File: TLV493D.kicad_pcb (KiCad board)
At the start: 2 copper layers, 6 parts, among them U1 TLV493D

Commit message: Add connector
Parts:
- added J1: Conn_01x04_Female, Connector_PinHeader_2.54mm:PinHeader_1x04_P2.54mm_Vertical, F.Cu at (162.0, 113.0)
- R1: value R_Small -> 330
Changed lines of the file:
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@@
-(kicad_pcb (version 20171130) (host pcbnew "(5.1.2-1)-1")
+(kicad_pcb (version 20171130) (host pcbnew "(5.1.4-0-10_14)")
   (general
     (thickness 1.6)
@@
     (tracks 0)
     (zones 0)
-    (modules 6)
+    (modules 7)
     (nets 6)
   )
   (page A4)
+  (title_block
+    (title TLV493D)
+    (date 2019-09-04)
+    (rev 0.1)
+    (company "Electronic Cats")
+    (comment 4 "Andres Sabas")
+  )
   (layers
     (0 F.Cu signal)
@@
       (effects (font (size 1 1) (thickness 0.15)))
     )
-    (fp_text value R_Small (at 0 1.75) (layer F.Fab)
+    (fp_text value 330 (at 0 1.75) (layer F.Fab)
       (effects (font (size 1 1) (thickness 0.15)))
     )
@@
       (at (xyz 0 0 0))
       (scale (xyz 1 1 1))
+      (rotate (xyz 0 0 0))
+    )
+  )
+  (module Connector_PinHeader_2.54mm:PinHeader_1x04_P2.54mm_Vertical (layer F.Cu)
+    (at 162 113.02 270)
+    (descr "Through hole straight pin header, 1x04, 2.54mm pitch, single row")
+    (tags "Through hole pin header THT 1x04 2.54mm single row")
+    (fp_text reference J1 (at 0 -2.33 90) (layer F.SilkS)
+      (effects (font (size 1 1) (thickness 0.15)))
+    )
+    (fp_text value Conn_01x04_Female (at 0 9.95 90) (layer F.Fab)
+      (effects (font (size 1 1) (thickness 0.15)))
+    )
+    (fp_line (start -0.635 -1.27) (end 1.27 -1.27) (layer F.Fab) (width 0.1))
+    (fp_line (start 1.27 -1.27) (end 1.27 8.89) (layer F.Fab) (width 0.1))
+    (fp_line (start 1.27 8.89) (end -1.27 8.89) (layer F.Fab) (width 0.1))
+    (fp_line (start -1.27 8.89) (end -1.27 -0.635) (layer F.Fab) (width 0.1))
+    (fp_line (start -1.27 -0.635) (end -0.635 -1.27) (layer F.Fab) (width 0.1))
+    (fp_line (start -1.33 8.95) (end 1.33 8.95) (layer F.SilkS) (width 0.12))
+    (fp_line (start -1.33 1.27) (end -1.33 8.95) (layer F.SilkS) (width 0.12))
+    (fp_line (start 1.33 1.27) (end 1.33 8.95) (layer F.SilkS) (width 0.12))
+    (fp_line (start -1.33 1.27) (end 1.33 1.27) (layer F.SilkS) (width 0.12))
+    (fp_line (start -1.33 0) (end -1.33 -1.33) (layer F.SilkS) (width 0.12))
+    (fp_line (start -1.33 -1.33) (end 0 -1.33) (layer F.SilkS) (width 0.12))
+    (fp_line (start -1.8 -1.8) (end -1.8 9.4) (layer F.CrtYd) (width 0.05))
+    (fp_line (start -1.8 9.4) (end 1.8 9.4) (layer F.CrtYd) (width 0.05))
+    (fp_line (start 1.8 9.4) (end 1.8 -1.8) (layer F.CrtYd) (width 0.05))
+    (fp_line (start 1.8 -1.8) (end -1.8 -1.8) (layer F.CrtYd) (width 0.05))
+    (fp_text user %R (at 0 3.81) (layer F.Fab)
+      (effects (font (size 1 1) (thickness 0.15)))
+    )
+    (pad 1 thru_hole rect (at 0 0 270) (size 1.7 1.7) (drill 1) (layers *.Cu *.Mask)
+      (net 5 /SDA))
+    (pad 2 thru_hole oval (at 0 2.54 270) (size 1.7 1.7) (drill 1) (layers *.Cu *.Mask)
+      (net 4 /SCL))
+    (pad 3 thru_hole oval (at 0 5.08 270) (size 1.7 1.7) (drill 1) (layers *.Cu *.Mask)
+      (net 1 GND))
+    (pad 4 thru_hole oval (at 0 7.62 270) (size 1.7 1.7) (drill 1) (layers *.Cu *.Mask)
+      (net 2 VCC))
+    (model ${KISYS3DMOD}/Connector_PinHeader_2.54mm.3dshapes/PinHeader_1x04_P2.54mm_Vertical.wrl
+      (at (xyz 0 0 0))
+      (scale (xyz 1 1 1))

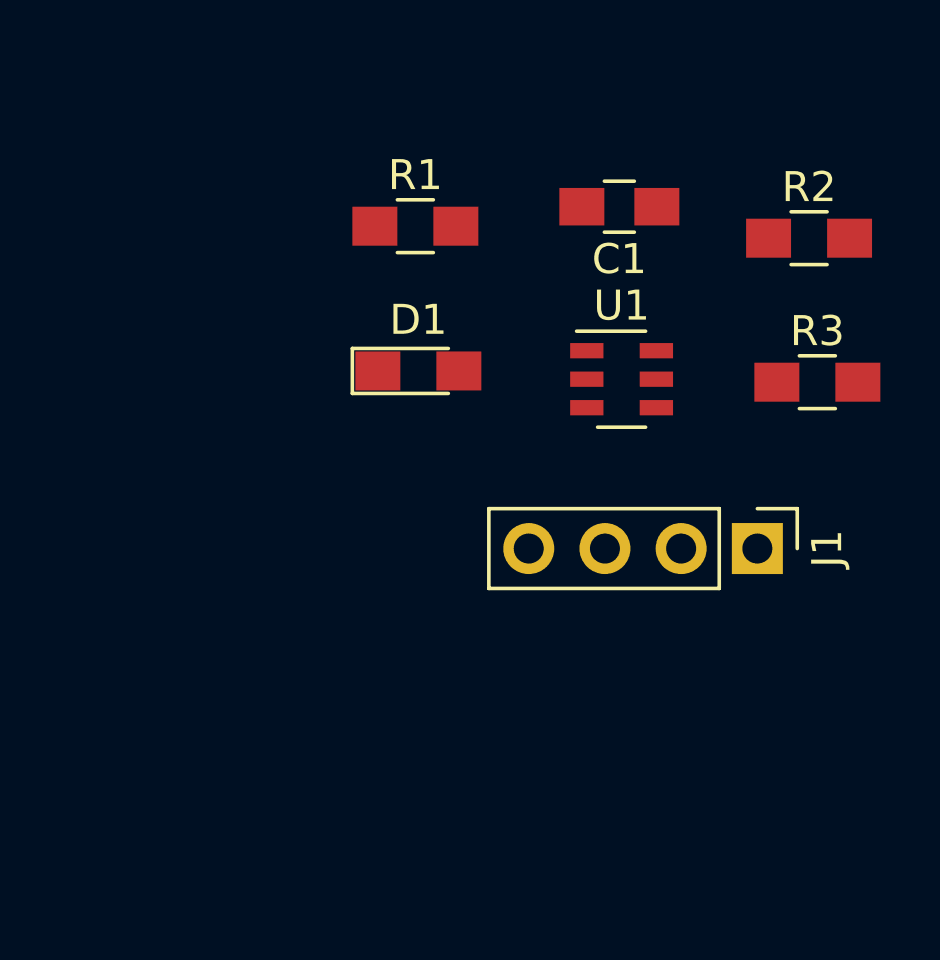
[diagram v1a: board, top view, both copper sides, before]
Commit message: Component order
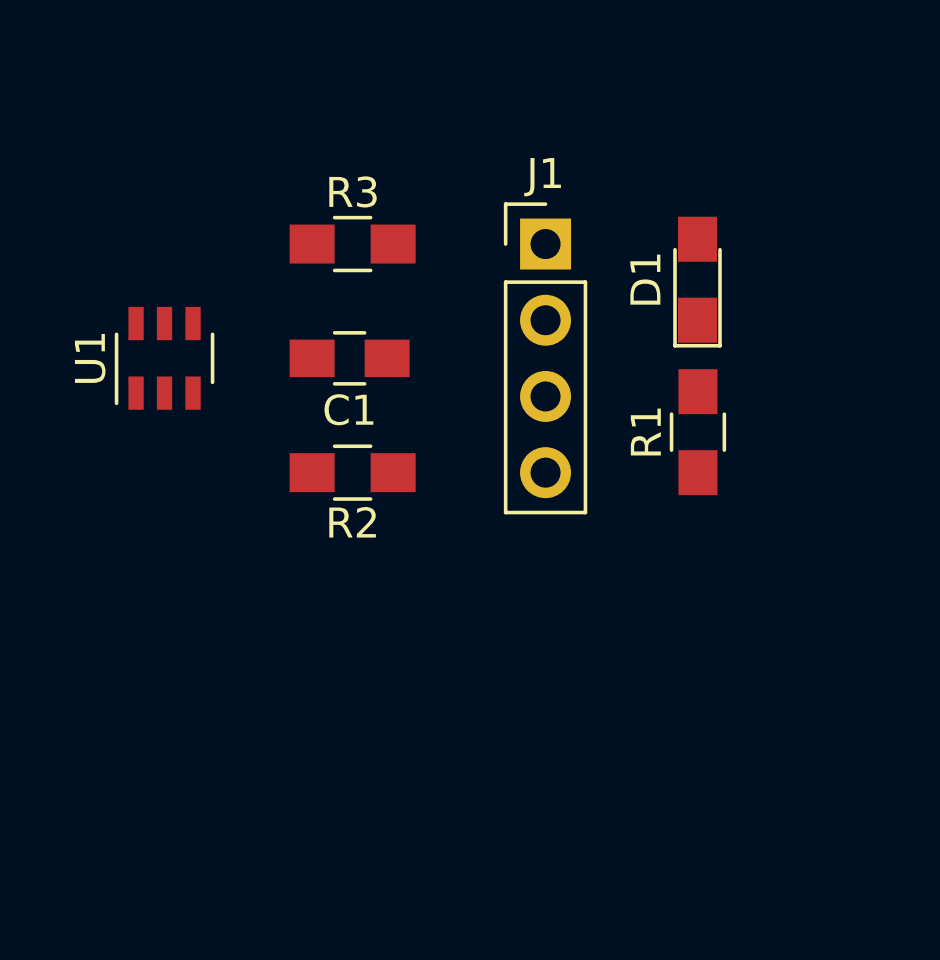
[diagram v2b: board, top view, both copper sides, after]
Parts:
- moved R2 17.1 mm to (148.5, 110.5), turned to 180 degrees
- moved R3 16.2 mm to (148.5, 102.9)
- moved U1 15.3 mm to (142.2, 106.7), turned to 90 degrees
- moved J1 12.4 mm to (154.9, 102.9), turned to 0 degrees
- moved R1 11.7 mm to (160.0, 109.1), turned to 90 degrees
- moved C1 10.3 mm to (148.4, 106.7)
- moved D1 9.79 mm to (160.0, 104.1), turned to 90 degrees
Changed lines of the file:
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@@
-(kicad_pcb (version 20171130) (host pcbnew "(5.1.4-0-10_14)")
+(kicad_pcb (version 20171130) (host pcbnew "(5.1.4)-1")
   (general
     (thickness 1.6)
@@
     (47 F.CrtYd user)
     (48 B.Fab user)
-    (49 F.Fab user)
+    (49 F.Fab user hide)
   )
   (setup
@@
     (solder_mask_min_width 0.25)
     (aux_axis_origin 0 0)
-    (visible_elements FFFFFF7F)
+    (visible_elements 7FFFFFFF)
     (pcbplotparams
       (layerselection 0x010fc_ffffffff)
@@
   )
   (module Capacitors_SMD:C_0805_HandSoldering (layer F.Cu)
-    (at 157.4 101.625 180)
+    (at 148.41 106.68 180)
     (descr "Capacitor SMD 0805, hand soldering")
     (tags "capacitor 0805")
@@
   )
   (module LEDs:LED_0805_HandSoldering (layer F.Cu)
-    (at 150.7 107.1)
+    (at 160.005 104.06 90)
     (descr "Resistor SMD 0805, hand soldering")
     (tags "resistor 0805")
     (attr smd)
-    (fp_text reference D1 (at 0 -1.7) (layer F.SilkS)
-      (effects (font (size 1 1) (thickness 0.15)))
-    )
-    (fp_text value LED (at 0 1.75) (layer F.Fab)
+    (fp_text reference D1 (at 0 -1.7 90) (layer F.SilkS)
+      (effects (font (size 1 1) (thickness 0.15)))
+    )
+    (fp_text value LED (at 0 1.75 90) (layer F.Fab)
       (effects (font (size 1 1) (thickness 0.15)))
     )
@@
     (fp_line (start -0.4 0) (end 0.2 -0.4) (layer F.Fab) (width 0.1))
     (fp_line (start -0.4 -0.4) (end -0.4 0.4) (layer F.Fab) (width 0.1))
-    (pad 2 smd rect (at 1.35 0) (size 1.5 1.3) (layers F.Cu F.Paste F.Mask)
+    (pad 2 smd rect (at 1.35 0 90) (size 1.5 1.3) (layers F.Cu F.Paste F.Mask)
       (net 3 "Net-(D1-Pad2)"))
-    (pad 1 smd rect (at -1.35 0) (size 1.5 1.3) (layers F.Cu F.Paste F.Mask)
+    (pad 1 smd rect (at -1.35 0 90) (size 1.5 1.3) (layers F.Cu F.Paste F.Mask)
       (net 1 GND))
     (model ${KISYS3DMOD}/LEDs.3dshapes/LED_0805.wrl
@@
   )
   (module Resistors_SMD:R_0805_HandSoldering (layer F.Cu)
-    (at 150.6 102.275)
+    (at 160.02 109.14 90)
     (descr "Resistor SMD 0805, hand soldering")
     (tags "resistor 0805")
     (attr smd)
-    (fp_text reference R1 (at 0 -1.7) (layer F.SilkS)
-      (effects (font (size 1 1) (thickness 0.15)))
-    )
-    (fp_text value 330 (at 0 1.75) (layer F.Fab)
+    (fp_text reference R1 (at 0 -1.7 90) (layer F.SilkS)
+      (effects (font (size 1 1) (thickness 0.15)))
+    )
+    (fp_text value 330 (at 0 1.75 90) (layer F.Fab)
       (effects (font (size 1 1) (thickness 0.15)))
     )
@@
     (fp_line (start 1 0.62) (end -1 0.62) (layer F.Fab) (width 0.1))
     (fp_line (start -1 0.62) (end -1 -0.62) (layer F.Fab) (width 0.1))
-    (fp_text user %R (at 0 0) (layer F.Fab)
+    (fp_text user %R (at 0 0 90) (layer F.Fab)
       (effects (font (size 0.5 0.5) (thickness 0.075)))
     )
-    (pad 2 smd rect (at 1.35 0) (size 1.5 1.3) (layers F.Cu F.Paste F.Mask)
+    (pad 2 smd rect (at 1.35 0 90) (size 1.5 1.3) (layers F.Cu F.Paste F.Mask)
       (net 3 "Net-(D1-Pad2)"))
-    (pad 1 smd rect (at -1.35 0) (size 1.5 1.3) (layers F.Cu F.Paste F.Mask)
+    (pad 1 smd rect (at -1.35 0 90) (size 1.5 1.3) (layers F.Cu F.Paste F.Mask)
       (net 2 VCC))
     (model ${KISYS3DMOD}/Resistors_SMD.3dshapes/R_0805.wrl
@@
   )
   (module Resistors_SMD:R_0805_HandSoldering (layer F.Cu)
-    (at 163.725 102.675)
+    (at 148.51 110.49 180)
     (descr "Resistor SMD 0805, hand soldering")
     (tags "resistor 0805")
@@
       (effects (font (size 0.5 0.5) (thickness 0.075)))
     )
-    (pad 2 smd rect (at 1.35 0) (size 1.5 1.3) (layers F.Cu F.Paste F.Mask)
+    (pad 2 smd rect (at 1.35 0 180) (size 1.5 1.3) (layers F.Cu F.Paste F.Mask)
       (net 4 /SCL))
-    (pad 1 smd rect (at -1.35 0) (size 1.5 1.3) (layers F.Cu F.Paste F.Mask)
+    (pad 1 smd rect (at -1.35 0 180) (size 1.5 1.3) (layers F.Cu F.Paste F.Mask)
       (net 2 VCC))
     (model ${KISYS3DMOD}/Resistors_SMD.3dshapes/R_0805.wrl
@@
   )
   (module Resistors_SMD:R_0805_HandSoldering (layer F.Cu)
-    (at 164 107.475)
+    (at 148.51 102.87)
     (descr "Resistor SMD 0805, hand soldering")
     (tags "resistor 0805")
@@
   )
   (module Housings_SSOP:TSOP-6_1.65x3.05mm_Pitch0.95mm (layer F.Cu)
-    (at 157.475 107.375)
+    (at 142.24 106.68 90)
     (descr "TSOP-6 package (comparable to TSOT-23), https://www.vishay.com/docs/71200/71200.pdf")
     (tags "Jedec MO-193C TSOP-6L")
     (attr smd)
-    (fp_text reference U1 (at 0 -2.45) (layer F.SilkS)
-      (effects (font (size 1 1) (thickness 0.15)))
-    )
-    (fp_text value TLV493D (at 0 2.5) (layer F.Fab)
+    (fp_text reference U1 (at 0 -2.45 90) (layer F.SilkS)
+      (effects (font (size 1 1) (thickness 0.15)))
+    )
+    (fp_text value TLV493D (at 0 2.5 90) (layer F.Fab)
       (effects (font (size 1 1) (thickness 0.15)))
     )
@@
     (fp_line (start 0.8 -1.6) (end -1.5 -1.6) (layer F.SilkS) (width 0.12))
     (fp_line (start -0.8 1.6) (end 0.8 1.6) (layer F.SilkS) (width 0.12))
-    (fp_text user %R (at 0 0 90) (layer F.Fab)
+    (fp_text user %R (at 0 0) (layer F.Fab)
       (effects (font (size 0.5 0.5) (thickness 0.075)))
     )
-    (pad 6 smd rect (at 1.16 -0.95) (size 1.11 0.51) (layers F.Cu F.Paste F.Mask)
+    (pad 6 smd rect (at 1.16 -0.95 90) (size 1.11 0.51) (layers F.Cu F.Paste F.Mask)
       (net 5 /SDA))
-    (pad 5 smd rect (at 1.16 0) (size 1.11 0.51) (layers F.Cu F.Paste F.Mask)
-      (net 1 GND))
-    (pad 4 smd rect (at 1.16 0.95) (size 1.11 0.51) (layers F.Cu F.Paste F.Mask)
-      (net 2 VCC))
-    (pad 3 smd rect (at -1.16 0.95) (size 1.11 0.51) (layers F.Cu F.Paste F.Mask)
-      (net 1 GND))
-    (pad 2 smd rect (at -1.16 0) (size 1.11 0.51) (layers F.Cu F.Paste F.Mask)
-      (net 1 GND))
-    (pad 1 smd rect (at -1.16 -0.95) (size 1.11 0.51) (layers F.Cu F.Paste F.Mask)
+    (pad 5 smd rect (at 1.16 0 90) (size 1.11 0.51) (layers F.Cu F.Paste F.Mask)
+      (net 1 GND))
+    (pad 4 smd rect (at 1.16 0.95 90) (size 1.11 0.51) (layers F.Cu F.Paste F.Mask)
+      (net 2 VCC))
+    (pad 3 smd rect (at -1.16 0.95 90) (size 1.11 0.51) (layers F.Cu F.Paste F.Mask)
+      (net 1 GND))
+    (pad 2 smd rect (at -1.16 0 90) (size 1.11 0.51) (layers F.Cu F.Paste F.Mask)
+      (net 1 GND))
+    (pad 1 smd rect (at -1.16 -0.95 90) (size 1.11 0.51) (layers F.Cu F.Paste F.Mask)
       (net 4 /SCL))
     (model ${KISYS3DMOD}/Housings_SSOP.3dshapes/TSOP-6_1.65x3.05mm_Pitch0.95mm.wrl
@@
   )
   (module Connector_PinHeader_2.54mm:PinHeader_1x04_P2.54mm_Vertical (layer F.Cu)
-    (at 162 113.02 270)
+    (at 154.94 102.87)
     (descr "Through hole straight pin header, 1x04, 2.54mm pitch, single row")
     (tags "Through hole pin header THT 1x04 2.54mm single row")
-    (fp_text reference J1 (at 0 -2.33 90) (layer F.SilkS)
-      (effects (font (size 1 1) (thickness 0.15)))
-    )
-    (fp_text value Conn_01x04_Female (at 0 9.95 90) (layer F.Fab)
+    (fp_text reference J1 (at 0 -2.33) (layer F.SilkS)
+      (effects (font (size 1 1) (thickness 0.15)))
+    )
+    (fp_text value Conn_01x04_Female (at 0 9.95) (layer F.Fab)
       (effects (font (size 1 1) (thickness 0.15)))
     )
@@
     (fp_line (start 1.8 9.4) (end 1.8 -1.8) (layer F.CrtYd) (width 0.05))
     (fp_line (start 1.8 -1.8) (end -1.8 -1.8) (layer F.CrtYd) (width 0.05))
-    (fp_text user %R (at 0 3.81) (layer F.Fab)
-      (effects (font (size 1 1) (thickness 0.15)))
-    )
-    (pad 1 thru_hole rect (at 0 0 270) (size 1.7 1.7) (drill 1) (layers *.Cu *.Mask)
+    (fp_text user %R (at 0 3.81 -270) (layer F.Fab)
+      (effects (font (size 1 1) (thickness 0.15)))
+    )
+    (pad 1 thru_hole rect (at 0 0) (size 1.7 1.7) (drill 1) (layers *.Cu *.Mask)
       (net 5 /SDA))
-    (pad 2 thru_hole oval (at 0 2.54 270) (size 1.7 1.7) (drill 1) (layers *.Cu *.Mask)
+    (pad 2 thru_hole oval (at 0 2.54) (size 1.7 1.7) (drill 1) (layers *.Cu *.Mask)
       (net 4 /SCL))
-    (pad 3 thru_hole oval (at 0 5.08 270) (size 1.7 1.7) (drill 1) (layers *.Cu *.Mask)
-      (net 1 GND))
-    (pad 4 thru_hole oval (at 0 7.62 270) (size 1.7 1.7) (drill 1) (layers *.Cu *.Mask)
+    (pad 3 thru_hole oval (at 0 5.08) (size 1.7 1.7) (drill 1) (layers *.Cu *.Mask)
+      (net 1 GND))
+    (pad 4 thru_hole oval (at 0 7.62) (size 1.7 1.7) (drill 1) (layers *.Cu *.Mask)
       (net 2 VCC))
     (model ${KISYS3DMOD}/Connector_PinHeader_2.54mm.3dshapes/PinHeader_1x04_P2.54mm_Vertical.wrl

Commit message: rotate pcb
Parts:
- moved J1 13.4 mm to (157.9, 116.0), turned to 270 degrees
- moved U1 13.0 mm to (154.3, 102.0), turned to 0 degrees
- moved R3 11.0 mm to (158.1, 108.2), turned to 270 degrees
- moved D1 9.06 mm to (156.8, 112.5), turned to 0 degrees
- moved R1 8.97 mm to (151.7, 112.5), turned to 0 degrees
- moved C1 6.07 mm to (154.3, 108.1), turned to 90 degrees
- moved R2 3.02 mm to (150.5, 108.2), turned to 90 degrees

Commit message: contour
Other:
- board outline added: 14 x 26.7 mm
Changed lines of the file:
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@@
-(kicad_pcb (version 20171130) (host pcbnew "(5.1.4-0-10_14)")
+(kicad_pcb (version 20171130) (host pcbnew "(5.1.4)-1")
   (general
     (thickness 1.6)
-    (drawings 0)
+    (drawings 11)
     (tracks 0)
     (zones 0)
@@
     )
   )
+  (gr_line (start 146.89 124.62) (end 160.89 124.65) (layer Edge.Cuts) (width 0.05))
+  (gr_line (start 146.9 105) (end 146.89 124.62) (layer Edge.Cuts) (width 0.05))
+  (dimension 13.900176 (width 0.15) (layer Dwgs.User)
+    (gr_text "13.900 mm" (at 153.936806 127.284899 -0.2885374576) (layer Dwgs.User)
+      (effects (font (size 1 1) (thickness 0.15)))
+    )
+    (feature1 (pts (xy 147 124.63) (xy 146.9904 126.536329)))
+    (feature2 (pts (xy 160.9 124.7) (xy 160.8904 126.606329)))
+    (crossbar (pts (xy 160.893353 126.019915) (xy 146.993353 125.949915)))
+    (arrow1a (pts (xy 146.993353 125.949915) (xy 148.122796 125.369175)))
+    (arrow1b (pts (xy 146.993353 125.949915) (xy 148.116889 126.542001)))
+    (arrow2a (pts (xy 160.893353 126.019915) (xy 159.769817 125.427829)))
+    (arrow2b (pts (xy 160.893353 126.019915) (xy 159.76391 126.600655)))
+  )
+  (dimension 13.90036 (width 0.15) (layer Dwgs.User)
+    (gr_text "13.900 mm" (at 154.01187 96.430053 -0.4121927414) (layer Dwgs.User)
+      (effects (font (size 1 1) (thickness 0.15)))
+    )
+    (feature1 (pts (xy 147 104.98) (xy 147.056737 97.093613)))
+    (feature2 (pts (xy 160.9 105.08) (xy 160.956737 97.193613)))
+    (crossbar (pts (xy 160.952518 97.780019) (xy 147.052518 97.680019)))
+    (arrow1a (pts (xy 147.052518 97.680019) (xy 148.183211 97.101718)))
+    (arrow1b (pts (xy 147.052518 97.680019) (xy 148.174774 98.274529)))
+    (arrow2a (pts (xy 160.952518 97.780019) (xy 159.830262 97.185509)))
+    (arrow2b (pts (xy 160.952518 97.780019) (xy 159.821825 98.35832)))
+  )
+  (gr_line (start 150 98) (end 146.9 105) (layer Edge.Cuts) (width 0.05))
+  (dimension 13.038405 (width 0.12) (layer F.SilkS)
+    (gr_text "13.038 mm" (at 154.47889 104.609685 32.47119229) (layer F.SilkS)
+      (effects (font (size 1 1) (thickness 0.15)))
+    )
+    (feature1 (pts (xy 147 105) (xy 148.611893 107.532975)))
+    (feature2 (pts (xy 158 98) (xy 159.611893 100.532975)))
+    (crossbar (pts (xy 159.297058 100.038235) (xy 148.297058 107.038235)))
+    (arrow1a (pts (xy 148.297058 107.038235) (xy 148.932611 105.938702)))
+    (arrow1b (pts (xy 148.297058 107.038235) (xy 149.562281 106.928183)))
+    (arrow2a (pts (xy 159.297058 100.038235) (xy 158.031835 100.148287)))
+    (arrow2b (pts (xy 159.297058 100.038235) (xy 158.661505 101.137768)))
+  )
+  (dimension 13.008459 (width 0.12) (layer F.SilkS)
+    (gr_text "13.008 mm" (at 154.734599 102.648292 -33.07926146) (layer F.SilkS)
+      (effects (font (size 1 1) (thickness 0.15)))
+    )
+    (feature1 (pts (xy 150 98) (xy 149.657695 98.52551)))
+    (feature2 (pts (xy 160.9 105.1) (xy 160.557695 105.62551)))
+    (crossbar (pts (xy 160.877763 105.134138) (xy 149.977763 98.034138)))
+    (arrow1a (pts (xy 149.977763 98.034138) (xy 151.241747 98.157611)))
+    (arrow1b (pts (xy 149.977763 98.034138) (xy 150.601611 99.140354)))
+    (arrow2a (pts (xy 160.877763 105.134138) (xy 160.253915 104.027922)))
+    (arrow2b (pts (xy 160.877763 105.134138) (xy 159.613779 105.010665)))
+  )
+  (gr_line (start 160.9 123) (end 160.9 124.7) (layer Edge.Cuts) (width 0.05))
+  (gr_line (start 160.9 105.1) (end 160.9 123) (layer Edge.Cuts) (width 0.05))
+  (gr_line (start 158 98) (end 160.9 105.1) (layer Edge.Cuts) (width 0.05))
+  (gr_line (start 150 98) (end 158 98) (layer Edge.Cuts) (width 0.05))
 )

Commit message: fix edge
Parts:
- moved U1 0.29 mm to (154.0, 102.0)
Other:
- board size 14 x 26.7 mm -> 14 x 20 mm
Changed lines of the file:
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@@
-(kicad_pcb (version 20171130) (host pcbnew "(5.1.4)-1")
+(kicad_pcb (version 20171130) (host pcbnew "(5.1.4-0-10_14)")
   (general
     (thickness 1.6)
-    (drawings 11)
+    (drawings 10)
     (tracks 0)
     (zones 0)
@@
   )
   (module Housings_SSOP:TSOP-6_1.65x3.05mm_Pitch0.95mm (layer F.Cu)
-    (at 154.31 101.95)
+    (at 154.02 101.97)
     (descr "TSOP-6 package (comparable to TSOT-23), https://www.vishay.com/docs/71200/71200.pdf")
     (tags "Jedec MO-193C TSOP-6L")
@@
     )
   )
-  (gr_line (start 146.89 124.62) (end 160.89 124.65) (layer Edge.Cuts) (width 0.05))
-  (gr_line (start 146.9 105) (end 146.89 124.62) (layer Edge.Cuts) (width 0.05))
+  (gr_line (start 146.9 105) (end 146.94 117.97) (layer Edge.Cuts) (width 0.05))
+  (gr_line (start 146.94 117.97) (end 160.9 118) (layer Edge.Cuts) (width 0.05))
   (dimension 13.900176 (width 0.15) (layer Dwgs.User)
-    (gr_text "13.900 mm" (at 153.936806 127.284899 -0.2885374576) (layer Dwgs.User)
-      (effects (font (size 1 1) (thickness 0.15)))
-    )
-    (feature1 (pts (xy 147 124.63) (xy 146.9904 126.536329)))
-    (feature2 (pts (xy 160.9 124.7) (xy 160.8904 126.606329)))
-    (crossbar (pts (xy 160.893353 126.019915) (xy 146.993353 125.949915)))
-    (arrow1a (pts (xy 146.993353 125.949915) (xy 148.122796 125.369175)))
-    (arrow1b (pts (xy 146.993353 125.949915) (xy 148.116889 126.542001)))
-    (arrow2a (pts (xy 160.893353 126.019915) (xy 159.769817 125.427829)))
-    (arrow2b (pts (xy 160.893353 126.019915) (xy 159.76391 126.600655)))
+    (gr_text "13.900 mm" (at 153.993453 121.114984 -0.2885374576) (layer Dwgs.User)
+      (effects (font (size 1 1) (thickness 0.15)))
+    )
+    (feature1 (pts (xy 147.056647 118.460085) (xy 147.047047 120.366414)))
+    (feature2 (pts (xy 160.956647 118.530085) (xy 160.947047 120.436414)))
+    (crossbar (pts (xy 160.95 119.85) (xy 147.05 119.78)))
+    (arrow1a (pts (xy 147.05 119.78) (xy 148.179443 119.19926)))
+    (arrow1b (pts (xy 147.05 119.78) (xy 148.173536 120.372086)))
+    (arrow2a (pts (xy 160.95 119.85) (xy 159.826464 119.257914)))
+    (arrow2b (pts (xy 160.95 119.85) (xy 159.820557 120.43074)))
   )
   (dimension 13.90036 (width 0.15) (layer Dwgs.User)
@@
     (arrow2b (pts (xy 160.877763 105.134138) (xy 159.613779 105.010665)))
   )
-  (gr_line (start 160.9 123) (end 160.9 124.7) (layer Edge.Cuts) (width 0.05))
-  (gr_line (start 160.9 105.1) (end 160.9 123) (layer Edge.Cuts) (width 0.05))
+  (gr_line (start 160.9 105.1) (end 160.9 118) (layer Edge.Cuts) (width 0.05))
   (gr_line (start 158 98) (end 160.9 105.1) (layer Edge.Cuts) (width 0.05))
   (gr_line (start 150 98) (end 158 98) (layer Edge.Cuts) (width 0.05))
